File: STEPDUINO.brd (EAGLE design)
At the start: 113 x 73.7 mm, 140 parts, among them IC1 ATMEGA328P TQFP32, IC2 MC34063, IC3 LD111733 SOT-223, IC4 74HC4094, IC5 DRV8811, IC6 DRV8811, IC7 ATMEGA16U2-MU, IC8 LM358D, J1 12V Supply, J2 Touchscreen, P1 microSD, P2 ICSP:MAIN, P3 ICSP:USB, P4 USB-6PSMT, Q1 FDN340P, SW1 RESET

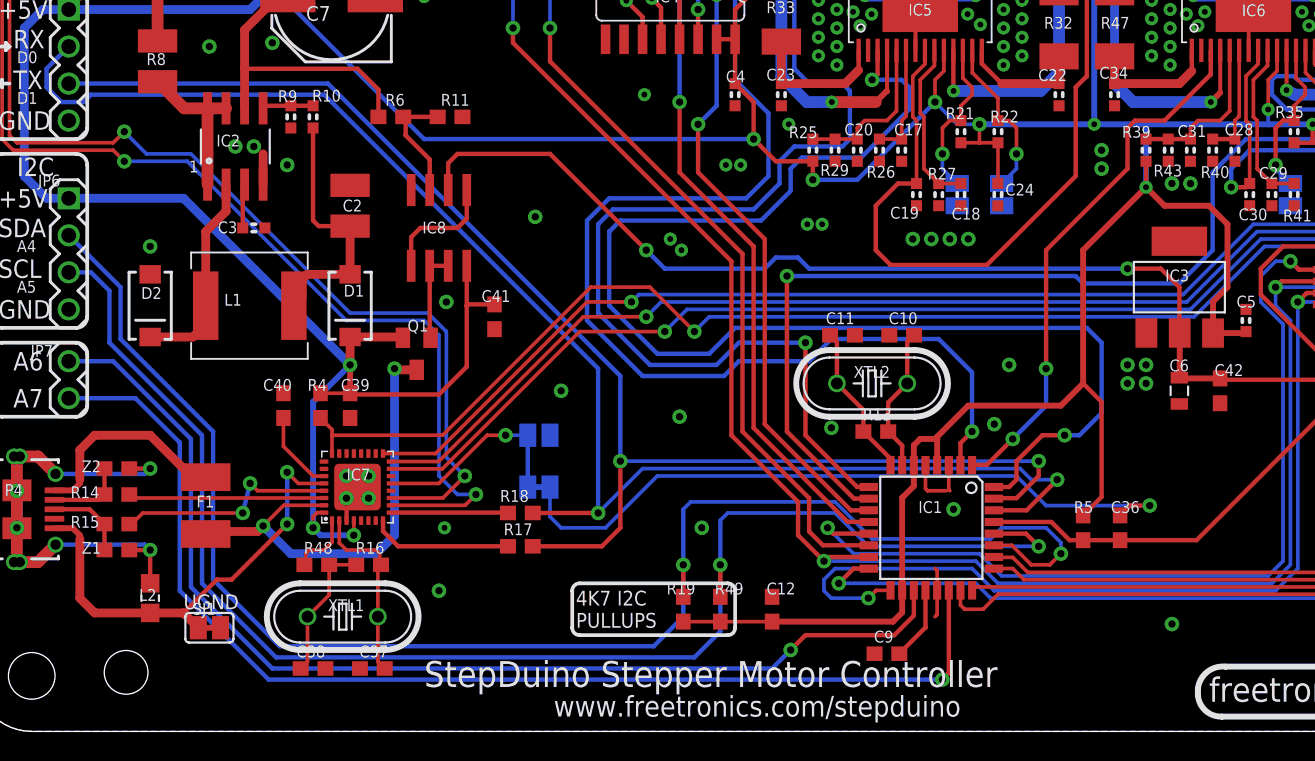
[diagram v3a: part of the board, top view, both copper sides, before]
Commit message: Made 0603 resistor and capacitor footprints consistent
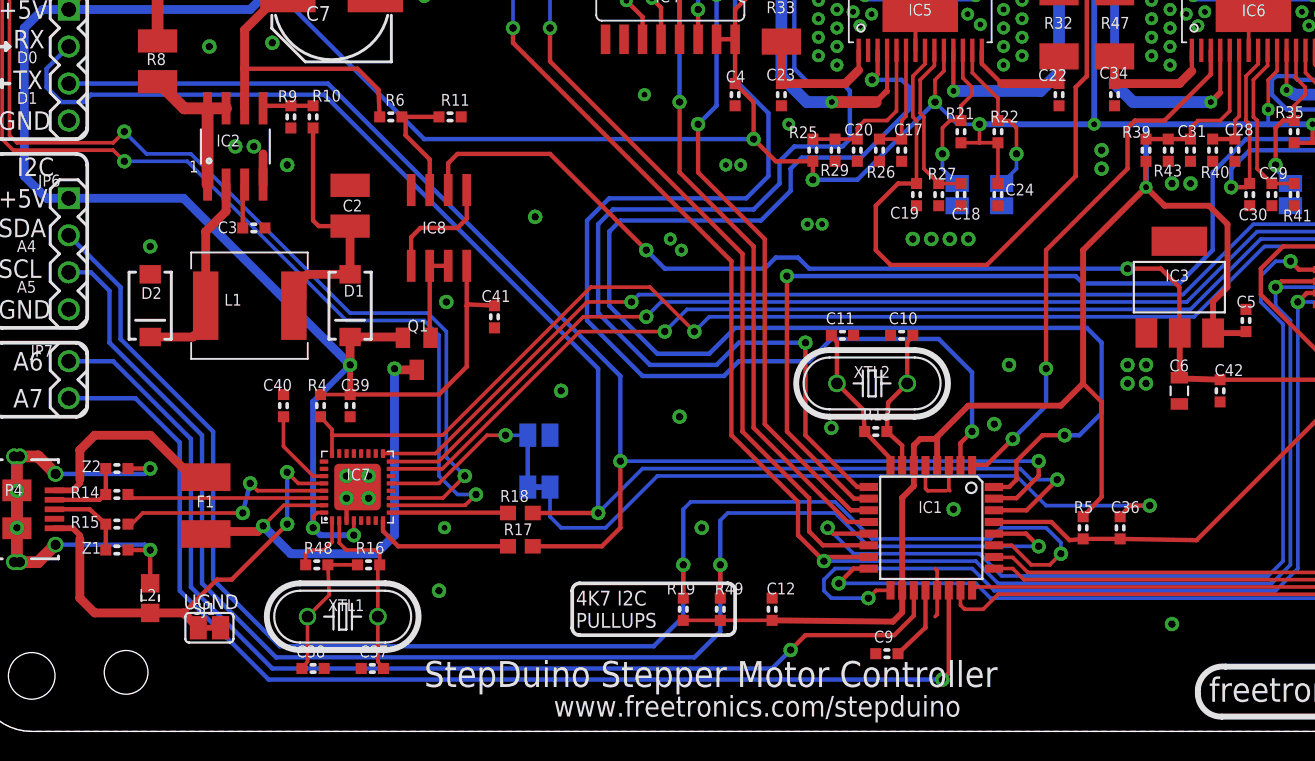
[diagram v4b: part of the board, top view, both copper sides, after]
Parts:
- C10, C11, C12, C36, C37, C38, C39, C40, C41, C42, R13, R14, R15, R16, R48, Z1, Z2: device freetronics:0603 -> freetronics-master-v1.1:0603
- C9, R11, R19, R4, R49, R5, R6: device freetronics:0603@1 -> freetronics-master-v1.1:0603
- R1, R2, R3, R7: device freetronics-master-v1:0603 -> freetronics-master-v1.1:0603
